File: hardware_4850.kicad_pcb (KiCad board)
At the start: 4 copper layers, 207.2 x 123 mm, 283 parts, among them J101 PWM, J102 ADC, J103 PWM, J104 ADC, J105 +, J106 A, J107 B, J108 C, J109 GND, J1101 HALL, J1102 PWM_EN, J1103 CAN_IN, J1104 CAN_Out, J501 Enable, J601 AIN, J602 USB_B_Mini, J701 MOT_TEMP, P1101 SWD, Q201 NCEP6080AG, Q202 NCEP6080AG, Q203 NCEP6080AG, Q204 NCEP6080AG, Q301 NCEP6080AG, Q302 NCEP6080AG, Q303 NCEP6080AG, Q304 NCEP6080AG, Q401 NCEP6080AG, Q402 NCEP6080AG, Q403 NCEP6080AG, Q404 NCEP6080AG, U1001 GS8632-MR, U1101 TCAN334, U1102 24LC04, U1103 AP2204K-5.0, U201 LM5109BMA, U202 INA240A1PWR, U301 LM5109BMA, U302 INA240A1PWR, U401 LM5109BMA, U402 INA240A1PWR, U501 LMR12010Y, U502 LM5008, U601 STM32F730R8Tx, U701 GS8632-MR, U801 GS8632-MR, U901 GS8632-MR, X601 SM44T

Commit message: started routing of logic board
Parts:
- C605: moved to B.Cu
- moved FB502 7.29 mm to (224.2, 106.2)
- moved R1101 2.51 mm to (192.5, 96.0)
- moved C610 1.69 mm to (213.5, 116.5)
- moved R1105 1.52 mm to (192.5, 94.0)
- moved C611 0.79 mm to (226.5, 120.5)
- moved C608 0.71 mm to (227.0, 103.8)
- moved C707 0.71 mm to (223.2, 103.0)
- moved C708 0.71 mm to (224.8, 103.0)
- moved C709 0.71 mm to (221.8, 103.0)
- moved C605 0.50 mm to (229.8, 111.0)
- turned C603 to 90 degrees
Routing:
- net GNDD: track 8.47 -> 46.4 mm, vias 14 -> 22
- net +12V: track 49.1 -> 82.2 mm, vias 0 -> 1
- net GNDA: track 0.00 -> 31.5 mm, vias 0 -> 1
- net /controller/USB_VBUS: track 0.00 -> 31.1 mm, vias 0 -> 2
- net +3V3: track 2.43 -> 28.2 mm, vias 8 -> 13
- net /controller/CAN_TX: track 0.00 -> 15.3 mm
- net +3.3VADC: track 0.00 -> 14.8 mm, vias 0 -> 1
- net /controller/CAN_RX: track 0.00 -> 12.3 mm
- net /controller/TMS-SWDIO: track 0.00 -> 9.79 mm
- net /controller/analog/IcAC: track 0.00 -> 7.26 mm
- net /controller/AIN_ACC: track 0.00 -> 6.64 mm
- net /controller/TDO-SWO: track 0.00 -> 6.43 mm
- net Net-(J602-Pad1): track 0.00 -> 6.19 mm, vias 0 -> 1
- net /controller/TCK-SWCLK: track 0.00 -> 5.73 mm
- net /controller/AIN_DCC: track 0.00 -> 5.72 mm
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
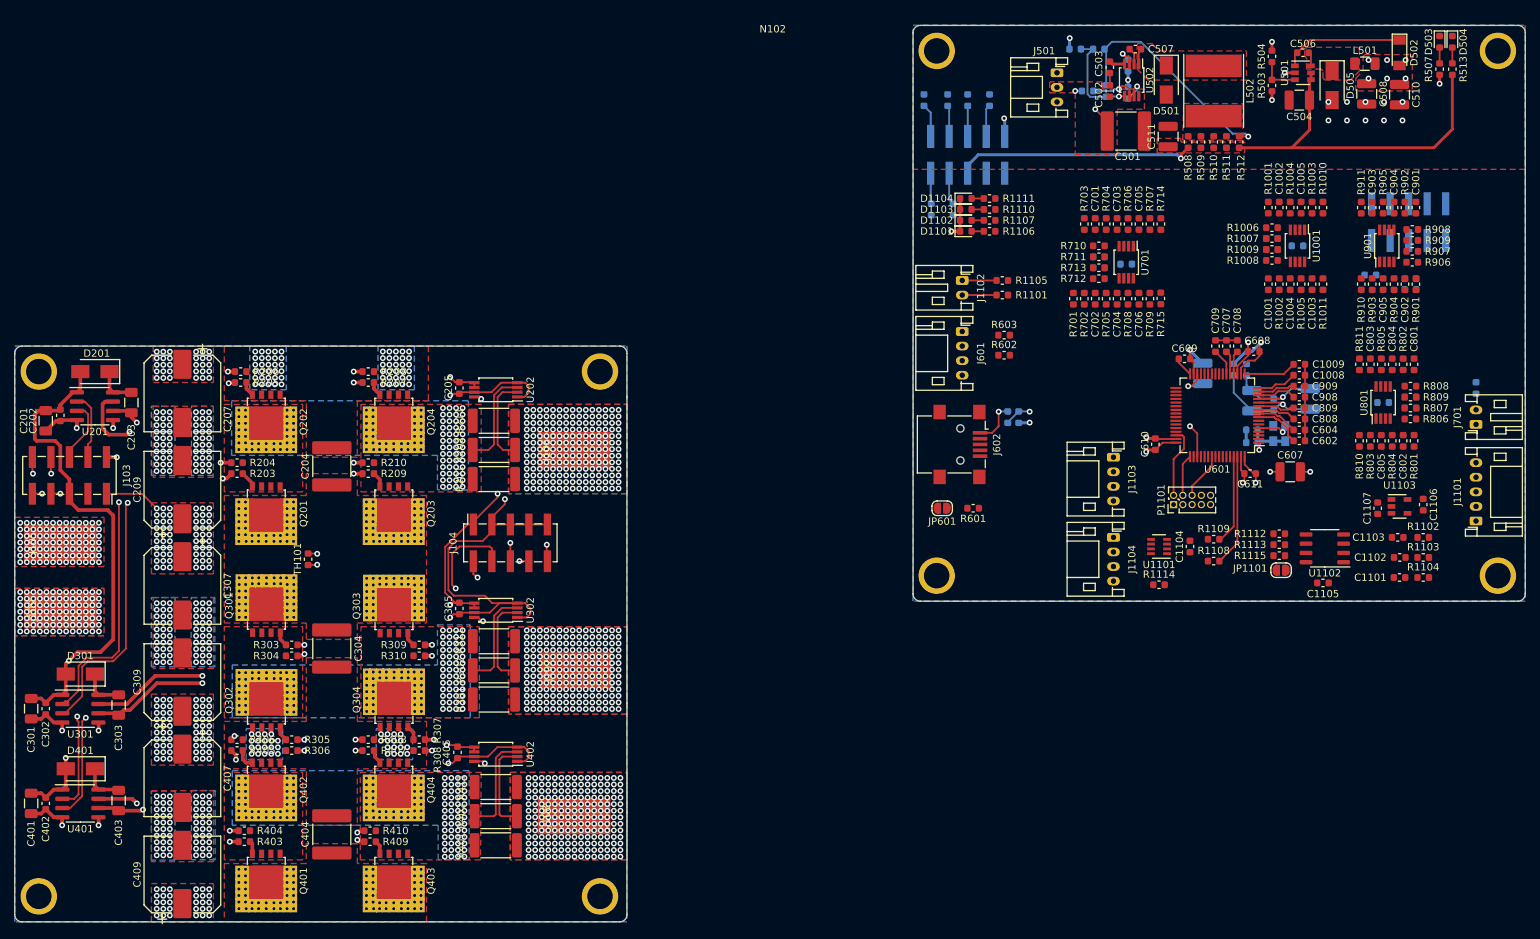
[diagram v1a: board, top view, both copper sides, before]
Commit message: added monting holes for coolplate
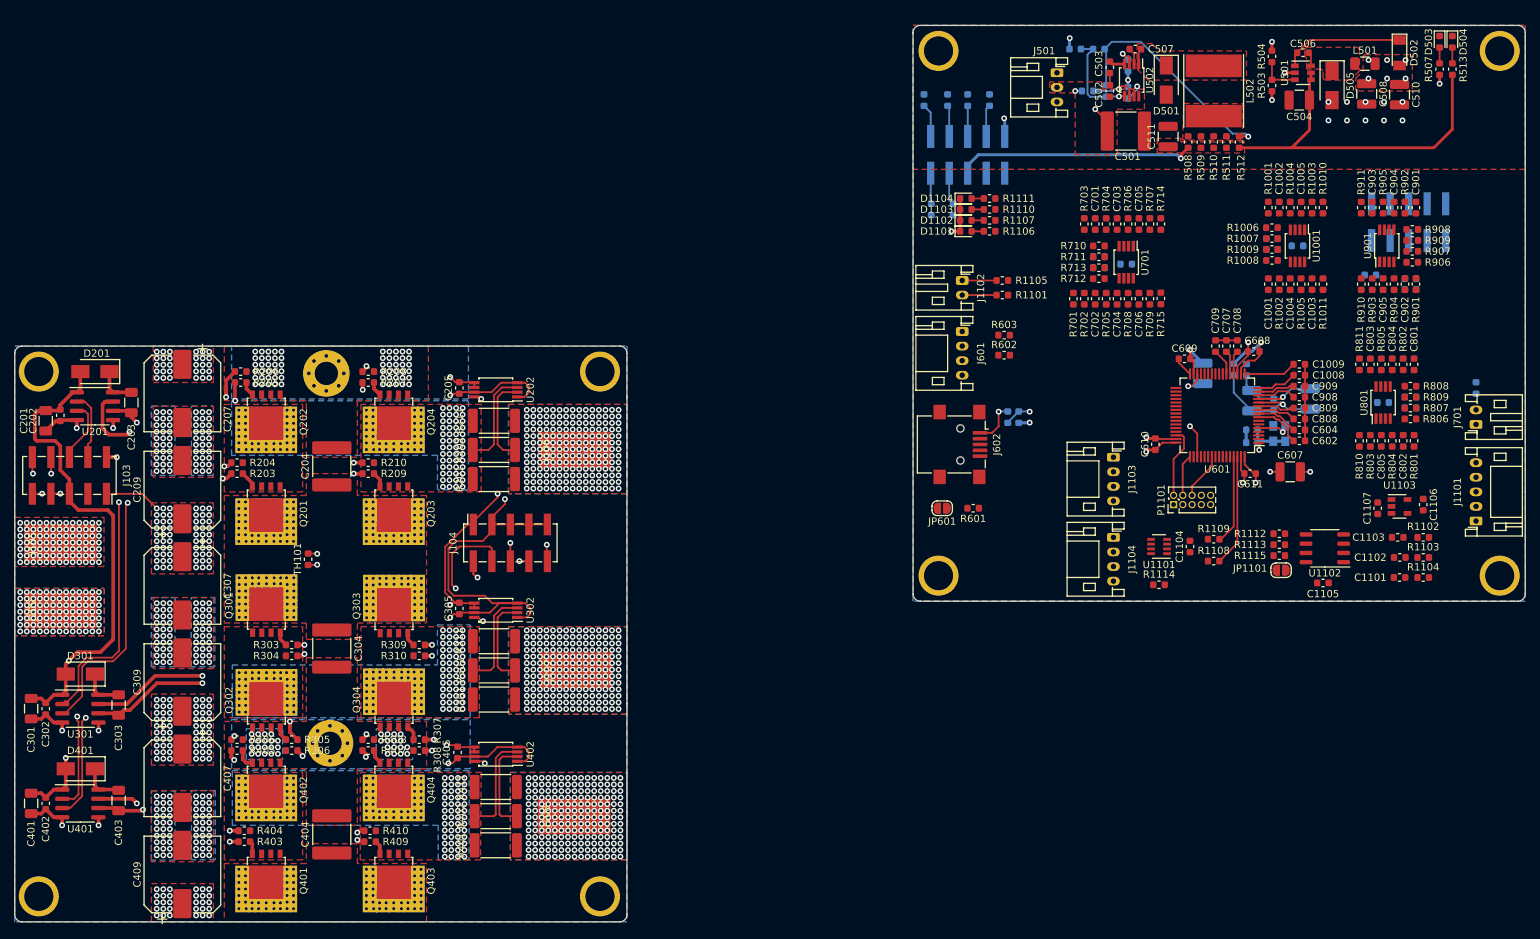
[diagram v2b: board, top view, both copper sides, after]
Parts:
- added H105: GND, MountingHole:MountingHole_3.2mm_M3_Pad_Via, F.Cu at (99.8, 106.8)
- added H106: GND, MountingHole:MountingHole_3.2mm_M3_Pad_Via, F.Cu at (100.2, 157.5)
- moved N102 0.25 mm to (170.8, 59.5)
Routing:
- net Net-(C401-Pad2): track 59.2 -> 63.5 mm
- net Net-(C201-Pad2): track 52.0 -> 56.2 mm
- net Net-(C301-Pad2): track 71.0 -> 75.1 mm
- net Net-(R305-Pad2): track 59.9 -> 63.2 mm
- net Net-(R405-Pad2): track 47.0 -> 49.1 mm
- net Net-(R205-Pad2): track 40.4 -> 42.1 mm
- net Net-(C203-Pad2): track 45.4 -> 44.4 mm

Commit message: routed someof the analog systems
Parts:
- moved R910 16.7 mm to (258.0, 98.5), turned to 180 degrees
- moved R911 15.6 mm to (247.5, 98.5), turned to 0 degrees
- moved R903 15.0 mm to (258.0, 97.0), turned to 0 degrees
- moved C903 13.7 mm to (247.5, 97.0), turned to 180 degrees
- moved R714 13.5 mm to (213.2, 99.8), turned to 0 degrees
- moved C905 13.3 mm to (258.0, 95.5), turned to 180 degrees
- moved R1010 12.8 mm to (235.8, 96.8), turned to 180 degrees
- moved R707 12.0 mm to (213.2, 98.2), turned to 0 degrees
- moved R905 11.8 mm to (247.5, 95.5), turned to 180 degrees
- moved R904 11.8 mm to (258.0, 94.0), turned to 0 degrees
- moved R715 11.7 mm to (203.0, 99.8), turned to 180 degrees
- moved R1011 11.5 mm to (225.2, 96.8), turned to 0 degrees
- moved R1003 11.3 mm to (235.8, 95.2), turned to 0 degrees
- moved C705 10.7 mm to (213.2, 96.8), turned to 0 degrees
- moved C902 10.4 mm to (258.0, 92.5), turned to 0 degrees
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- renumbered C1105 to Cm
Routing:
- net GNDA: track 31.5 -> 76.9 mm, vias 1 -> 2
- net +48V: track 0.00 -> 14.3 mm, vias 0 -> 1
- net +3.3VADC: track 14.8 -> 25.9 mm
- net Net-(C1002-Pad2): track 0.00 -> 6.80 mm
- net Net-(C704-Pad2): track 0.00 -> 6.63 mm
- net Net-(C703-Pad2): track 0.00 -> 6.63 mm
- net Net-(C1001-Pad1): track 0.00 -> 6.63 mm
- net Net-(C706-Pad1): track 0.00 -> 5.81 mm
- net Net-(C705-Pad1): track 0.00 -> 5.58 mm
- net Net-(C1005-Pad2): track 0.00 -> 5.46 mm
- net Net-(C1003-Pad1): track 0.00 -> 5.33 mm
- net Net-(C711-Pad1): track 0.00 -> 5.31 mm
- net Net-(C1005-Pad1): track 0.00 -> 5.03 mm
- net Net-(C1004-Pad1): track 0.00 -> 4.74 mm
- net Net-(C702-Pad2): track 0.00 -> 4.50 mm
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
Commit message: ..
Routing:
- net /controller/Ib: track 0.00 -> 18.7 mm, vias 0 -> 1
- net GNDA: track 76.9 -> 85.7 mm
- net Net-(C902-Pad2): track 0.00 -> 6.63 mm
- net Net-(C905-Pad2): track 0.00 -> 5.46 mm
- net Net-(C906-Pad2): track 0.00 -> 5.06 mm
- net Net-(C905-Pad1): track 0.00 -> 5.03 mm
- net Net-(C907-Pad2): track 0.00 -> 3.26 mm
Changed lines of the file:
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@@
     (thickness 1.6)
     (drawings 102)
-    (tracks 2452)
+    (tracks 2496)
     (zones 0)
     (modules 285)
@@
   (segment (start 210.725 94.025) (end 210.2 94.025) (width 0.25) (layer Top) (net 24))
   (segment (start 211 93.75) (end 210.725 94.025) (width 0.25) (layer Top) (net 24))
+  (segment (start 252 90.7125) (end 253.5 90.7125) (width 0.25) (layer Top) (net 24))
+  (segment (start 253.961612 91.174112) (end 253.5 90.7125) (width 0.25) (layer Top) (net 24))
+  (segment (start 254.26251 91.47501) (end 253.961612 91.174112) (width 0.25) (layer Top) (net 24))
+  (segment (start 255.431504 91.47501) (end 254.26251 91.47501) (width 0.25) (layer Top) (net 24))
+  (segment (start 255.80001 91.843516) (end 255.431504 91.47501) (width 0.25) (layer Top) (net 24))
+  (segment (start 255.80001 93.67499) (end 255.80001 91.843516) (width 0.25) (layer Top) (net 24))
+  (segment (start 255.45 94.025) (end 255.80001 93.67499) (width 0.25) (layer Top) (net 24))
+  (segment (start 254.95 94.025) (end 255.45 94.025) (width 0.25) (layer Top) (net 24))
+  (segment (start 255.994882 92.038388) (end 255.80001 91.843516) (width 0.25) (layer Top) (net 24))
+  (segment (start 256.750888 92.038388) (end 255.994882 92.038388) (width 0.25) (layer Top) (net 24))
+  (segment (start 257.2125 92.5) (end 256.750888 92.038388) (width 0.25) (layer Top) (net 24))
   (segment (start 230.75 110.25) (end 231 110) (width 0.25) (layer Top) (net 25))
   (segment (start 227.675 110.25) (end 230.75 110.25) (width 0.25) (layer Top) (net 25))
@@
   (segment (start 223.25 105.2875) (end 221.75 103.7875) (width 0.25) (layer Top) (net 39))
   (segment (start 223.25 106.825) (end 223.25 105.2875) (width 0.25) (layer Top) (net 39))
+  (segment (start 248.749112 90.538388) (end 248.2875 91) (width 0.25) (layer Top) (net 49))
+  (segment (start 249.33751 89.94999) (end 248.749112 90.538388) (width 0.25) (layer Top) (net 49))
+  (segment (start 256.73749 89.94999) (end 249.33751 89.94999) (width 0.25) (layer Top) (net 49))
+  (segment (start 257.2125 90.425) (end 256.73749 89.94999) (width 0.25) (layer Top) (net 49))
+  (segment (start 257.2125 91) (end 257.2125 90.425) (width 0.25) (layer Top) (net 49))
+  (via (at 245.75 86) (size 0.8) (drill 0.4) (layers Top BATT+&PHASE) (net 49))
+  (segment (start 248.2875 91) (end 248.2875 88.5375) (width 0.25) (layer Top) (net 49))
+  (segment (start 248.2875 88.5375) (end 245.75 86) (width 0.25) (layer Top) (net 49))
+  (segment (start 245.75 88.485) (end 245.71 88.525) (width 0.25) (layer BATT+&PHASE) (net 49))
+  (segment (start 245.75 86) (end 245.75 88.485) (width 0.25) (layer BATT+&PHASE) (net 49))
+  (segment (start 258.7875 91) (end 258.7875 92.5) (width 0.25) (layer Top) (net 51))
+  (segment (start 258.7875 92.5) (end 258.7875 94) (width 0.25) (layer Top) (net 51))
+  (segment (start 259.33751 94.55001) (end 258.7875 94) (width 0.25) (layer Top) (net 51))
+  (segment (start 259.55001 94.76251) (end 259.33751 94.55001) (width 0.25) (layer Top) (net 51))
+  (segment (start 258.7875 97) (end 259.55001 96.23749) (width 0.25) (layer Top) (net 51))
+  (segment (start 259.55001 96.23749) (end 259.55001 94.76251) (width 0.25) (layer Top) (net 51))
+  (segment (start 256.7375 95.975) (end 257.2125 95.5) (width 0.25) (layer Top) (net 54))
+  (segment (start 254.95 95.975) (end 256.7375 95.975) (width 0.25) (layer Top) (net 54))
+  (segment (start 257.2125 98.5) (end 257.2125 97) (width 0.25) (layer Top) (net 54))
+  (segment (start 257.2125 97) (end 257.2125 95.5) (width 0.25) (layer Top) (net 54))
+  (segment (start 258.7125 95.5) (end 257.2125 94) (width 0.25) (layer Top) (net 55))
+  (segment (start 258.7875 95.5) (end 258.7125 95.5) (width 0.25) (layer Top) (net 55))
+  (segment (start 257.2125 94.0375) (end 257.2125 94) (width 0.25) (layer Top) (net 55))
+  (segment (start 255.925 95.325) (end 257.2125 94.0375) (width 0.25) (layer Top) (net 55))
+  (segment (start 254.95 95.325) (end 255.925 95.325) (width 0.25) (layer Top) (net 55))
+  (segment (start 253.5 92.2875) (end 255 92.2875) (width 0.25) (layer Top) (net 56))
+  (segment (start 253.5 92.825) (end 253.5 92.2875) (width 0.25) (layer Top) (net 56))
+  (segment (start 253.5 94.2) (end 253.5 92.825) (width 0.25) (layer Top) (net 56))
+  (segment (start 253.975 94.675) (end 253.5 94.2) (width 0.25) (layer Top) (net 56))
+  (segment (start 254.95 94.675) (end 253.975 94.675) (width 0.25) (layer Top) (net 56))
+  (segment (start 250.5 92.2875) (end 252 92.2875) (width 0.25) (layer Top) (net 57))
+  (segment (start 250.55 92.3375) (end 250.5 92.2875) (width 0.25) (layer Top) (net 57))
+  (segment (start 250.55 94.025) (end 250.55 92.3375) (width 0.25) (layer Top) (net 57))
   (segment (start 232.000888 109.538388) (end 232.4625 110) (width 0.25) (layer Top) (net 58))
   (segment (start 230.322811 109.200011) (end 231.662511 109.200011) (width 0.25) (layer Top) (net 58))

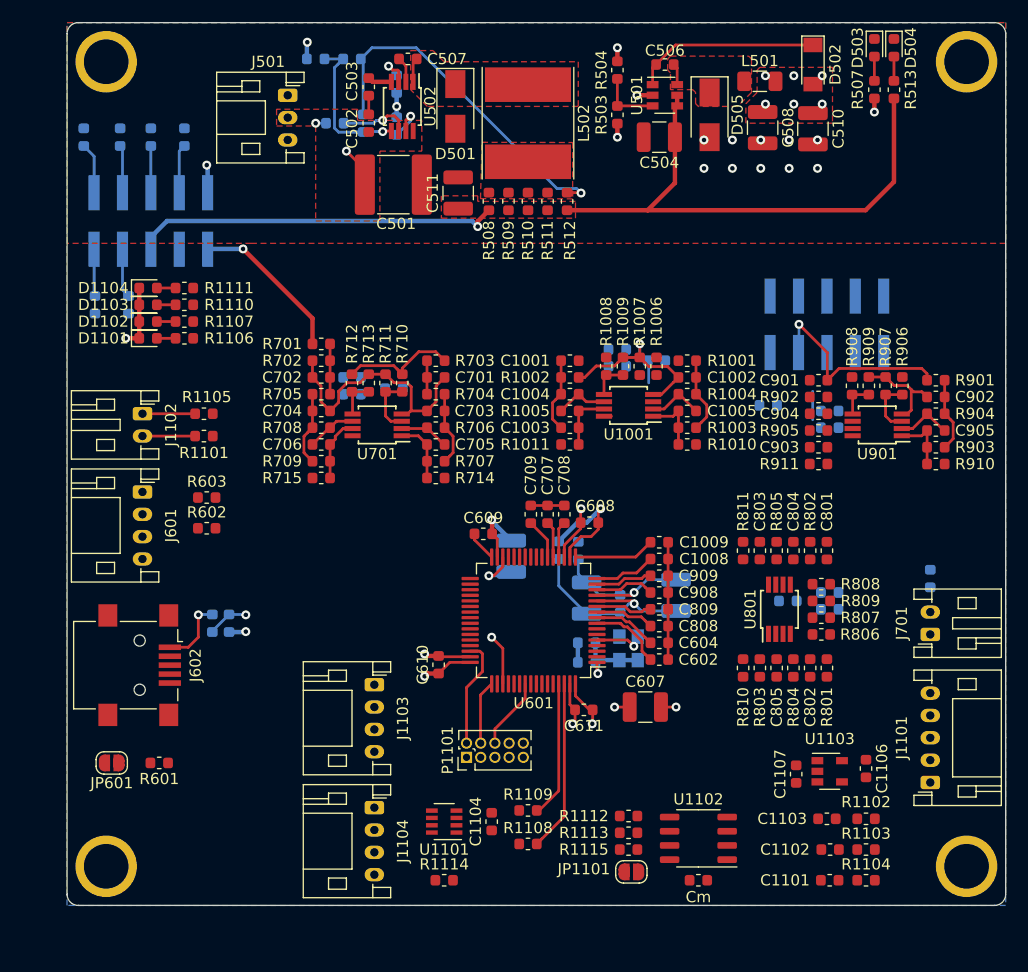
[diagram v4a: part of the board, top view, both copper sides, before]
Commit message: changed design rules or logic board to smaller wires
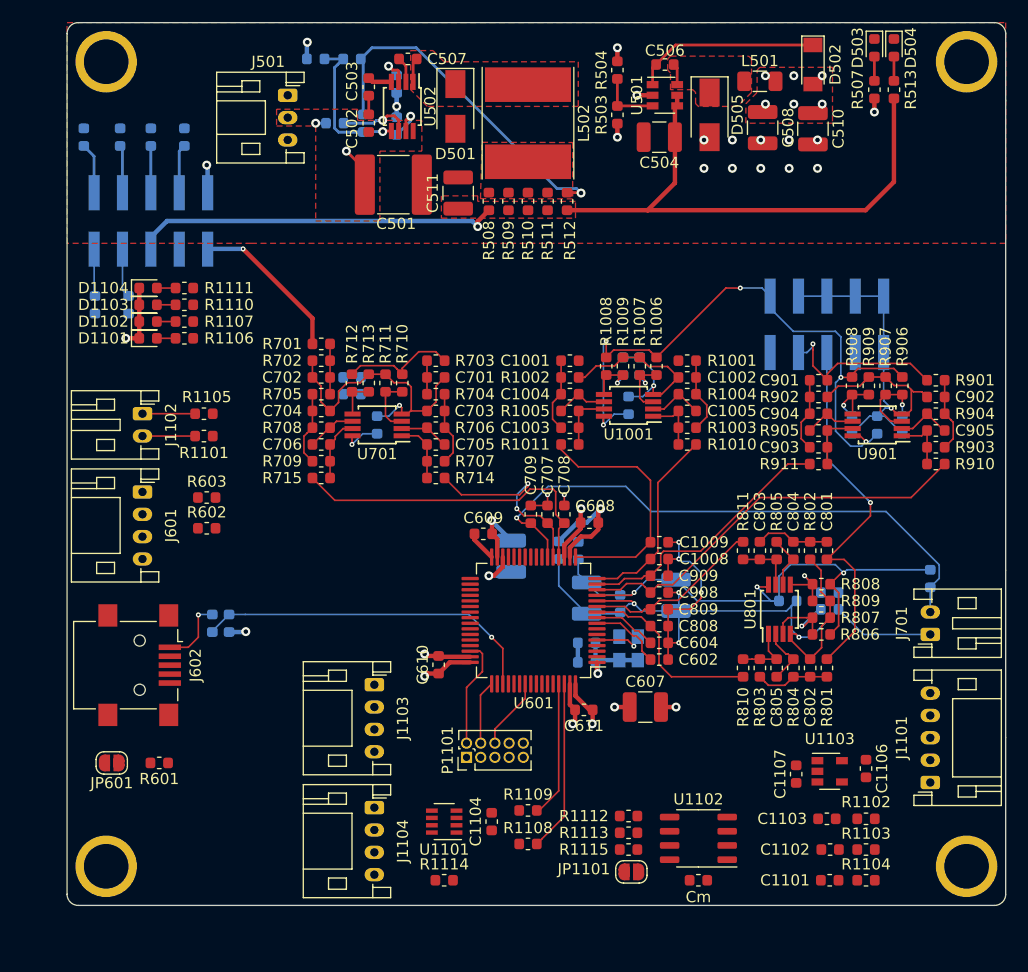
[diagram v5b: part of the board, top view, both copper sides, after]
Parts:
- moved C910 9.91 mm to (252.8, 95.0), turned to 90 degrees
- moved C906 6.50 mm to (255.0, 95.0), turned to 90 degrees
- moved C1010 4.72 mm to (230.5, 93.2), turned to 90 degrees
- moved C710 3.58 mm to (208.0, 95.0), turned to 90 degrees
- moved C1006 2.50 mm to (231.5, 89.8), turned to 270 degrees
- moved C907 2.36 mm to (250.5, 95.0), turned to 90 degrees
- moved C1007 0.50 mm to (230.0, 89.8), turned to 270 degrees
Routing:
- net +3.3VADC: track 25.9 -> 126.4 mm, vias 1 -> 9
- net GNDA: track 85.7 -> 177.8 mm, vias 2 -> 12
- net /controller/analog/MotTemp: track 3.66 -> 51.6 mm, vias 0 -> 1
- net /controller/Ia: track 0.00 -> 33.6 mm, vias 0 -> 1
- net /controller/analog/IbDC: track 5.35 -> 36.4 mm
- net /controller/analog/Vdc: track 3.24 -> 29.5 mm
- net /controller/analog/IbAC: track 5.10 -> 24.1 mm
- net /controller/analog/IcAC: track 7.26 -> 22.4 mm
- net /controller/analog/BrdgTemp: track 3.24 -> 17.8 mm, vias 0 -> 2
- net /controller/analog/IcDC: track 5.51 -> 17.5 mm
- net /controller/AIN_CUR_A: track 5.31 -> 17.0 mm
- net /controller/AIN_CUR_A_AC: track 5.08 -> 15.9 mm
- net Net-(C806-Pad2): track 0.00 -> 8.92 mm, vias 0 -> 1
- net Net-(C1006-Pad2): track 0.00 -> 6.74 mm, vias 0 -> 1
- net Net-(C807-Pad2): track 0.00 -> 6.66 mm, vias 0 -> 1
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- added copper zone on Inner_Top, net +3V3
- added copper zone on Inner_Bottom, net +BATT
- added copper zone on Inner_Bottom, net GNDD
- added copper zone on Inner_Bottom, net GNDPWR
- removed copper zone on B.Cu, net +3V3
- removed copper zone on GND, net +BATT
- removed copper zone on GND, net GNDD
- removed copper zone on GND, net GNDPWR
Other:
- net class Default: clearance 0.2 -> 0.15; trace_width 0.25 -> 0.15; via_dia 0.8 -> 0.45; via_drill 0.4 -> 0.2
- rule trace_clearance: 0.2 -> 0.15
- rule trace_min: 0.2 -> 0.1
- rule via_min_drill: 0.3 -> 0.2
- rule via_min_size: 0.4 -> 0.45

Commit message: routing..
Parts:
- moved C711 3.04 mm to (208.8, 91.2), turned to 90 degrees
- moved C712 1.80 mm to (207.2, 91.2), turned to 90 degrees
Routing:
- net Net-(R609-Pad2): track 0.00 -> 77.8 mm, vias 0 -> 1
- net Net-(R606-Pad2): track 0.00 -> 69.7 mm, vias 0 -> 1
- net Net-(R607-Pad2): track 0.00 -> 69.6 mm, vias 0 -> 1
- net Net-(R610-Pad2): track 0.00 -> 69.5 mm, vias 0 -> 1
- net GNDA: track 177.8 -> 230.6 mm, vias 12 -> 13
- net Net-(R611-Pad2): track 0.00 -> 52.7 mm, vias 0 -> 1
- net Net-(R608-Pad2): track 0.00 -> 50.2 mm, vias 0 -> 1
- net /controller/Temp+: track 3.00 -> 52.6 mm, vias 0 -> 1
- net +3.3VADC: track 126.4 -> 172.6 mm
- net /controller/interfaces/LED_PWM: track 0.00 -> 45.9 mm
- net /controller/interfaces/LED_MODE: track 0.00 -> 44.9 mm
- net /controller/interfaces/LED_ERROR: track 0.00 -> 43.6 mm
- net /controller/interfaces/LED_RUN: track 0.00 -> 40.1 mm
- net /controller/AIN_DCC: track 5.72 -> 44.3 mm, vias 0 -> 2
- net /controller/AIN_ACC: track 6.64 -> 44.3 mm, vias 0 -> 2
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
